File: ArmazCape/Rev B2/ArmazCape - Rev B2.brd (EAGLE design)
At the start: 85 x 70.5 mm, 167 parts, among them J2 85505-5113, Q1 32.768kHz, 12.5pF, Q2 ASE, Q4 IRLML6344TRPBF, Q5 IRLML6344TRPBF, U1 L7985A, U13 L7985A, U19 DS1307ZN+, U20 24AA256-I/SN, U5 CD4050BD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

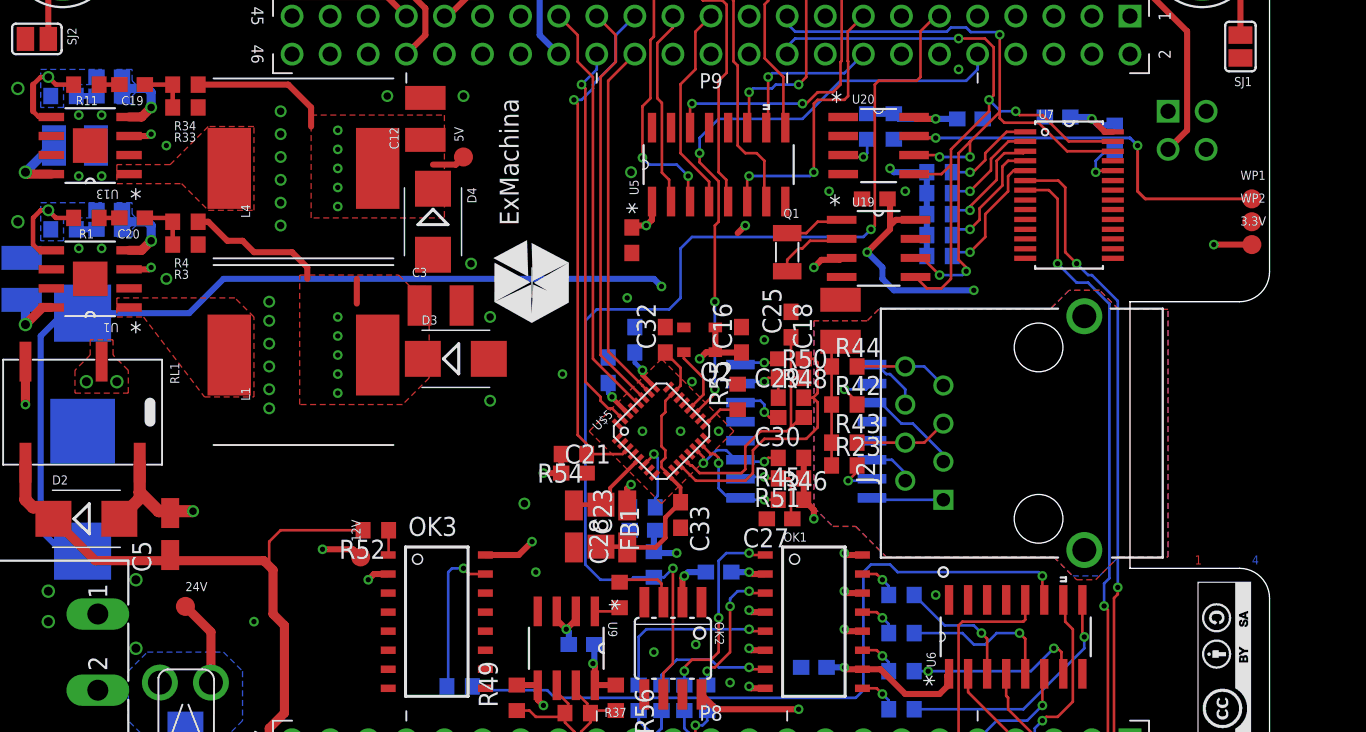
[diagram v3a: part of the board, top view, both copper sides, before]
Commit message: Updated ArmazCape - Rev B2: Silkscreen for production Fixed bad Rev number on board.
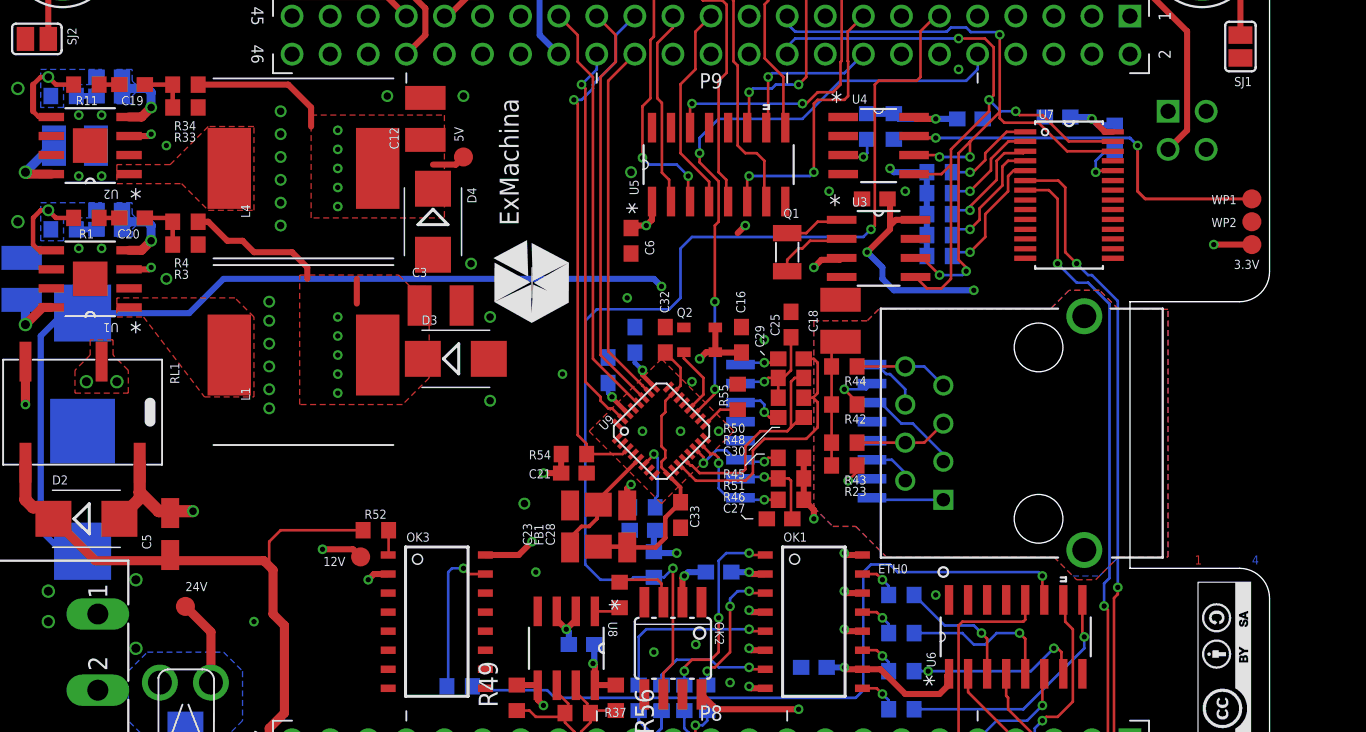
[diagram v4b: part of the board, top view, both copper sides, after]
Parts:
- removed U$5: KSZ8851SNLI, Micrel_By_element14_Batch_1:QFN50P500X500X85-32L
- added U8: SN65HVD08D, ti:SOIC127P600X175-8N
- U9: value SN65HVD08D -> KSZ8851SNLI; device ti:SOIC127P600X175-8N -> Micrel_By_element14_Batch_1:QFN50P500X500X85-32L
- moved U$3 228.5 mm to (-83.3, -55.6)
- moved U9 15.8 mm to (44.5, 34.3), turned to 45 degrees
- moved C23 0.25 mm to (38.4, 27.9), turned to 90 degrees
- moved FB1 0.18 mm to (40.2, 27.9)
- moved C6 0.07 mm to (42.4, 47.0)
- renumbered J2 to ETH0, U$4 to M1, U13 to U2, U19 to U3, U20 to U4
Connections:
- net +3V3: now also U9.25, U9.30; no longer U$5.25, U$5.30
- net +5V/1: now also U8.8; no longer U9.8
- net DMX0-A: now also U8.6; no longer U9.6
- net DMX0-B: now also U8.7; no longer U9.7
- net GND: now also U9.13, U9.18, U9.22, U9.24, U9.29, U9.4, U9.8; no longer U$5.13, U$5.18, U$5.22, U$5.24, U$5.29, U$5.4, U$5.8
- net GND1: now also U8.2, U8.3, U8.5; no longer U9.2, U9.3, U9.5
- net KSZ_X1: now also U9.20; no longer U$5.20
- net N$2000: now also U9.11; no longer U$5.11
- net N$27: now also U8.1; no longer U9.1
- net N$300: now also U9.12; no longer U$5.12
- net N$38: now also U9.17; no longer U$5.17
- net N$4200: now also U9.14; no longer U$5.14
- net N$4400: now also U9.15; no longer U$5.15
- net N$52: now also U9.6; no longer U$5.6
- net SPI1_CS0: now also U9.26; no longer U$5.26
- net SPI1_INT: now also U9.3; no longer U$5.3
- net SPI1_MISO: now also U9.27; no longer U$5.27
- net SPI1_MOSI: now also U9.31; no longer U$5.31
- net SPI1_SCLK: now also U9.28; no longer U$5.28
- net SYS_RESET: now also U9.19; no longer U$5.19
- net VDD18CORE: now also U9.5; no longer U$5.5
- net VDD18PLL: now also U9.23, U9.9; no longer U$5.23, U$5.9
- net VDD_A3.3: now also U9.16; no longer U$5.16
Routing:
- net VDD18CORE: track 5.88 -> 8.06 mm
- removed copper zone on layer 15, net GND
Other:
- board text added: "ArmazCape Rev B2"
- board text removed: "ArmazCape Rev B1"

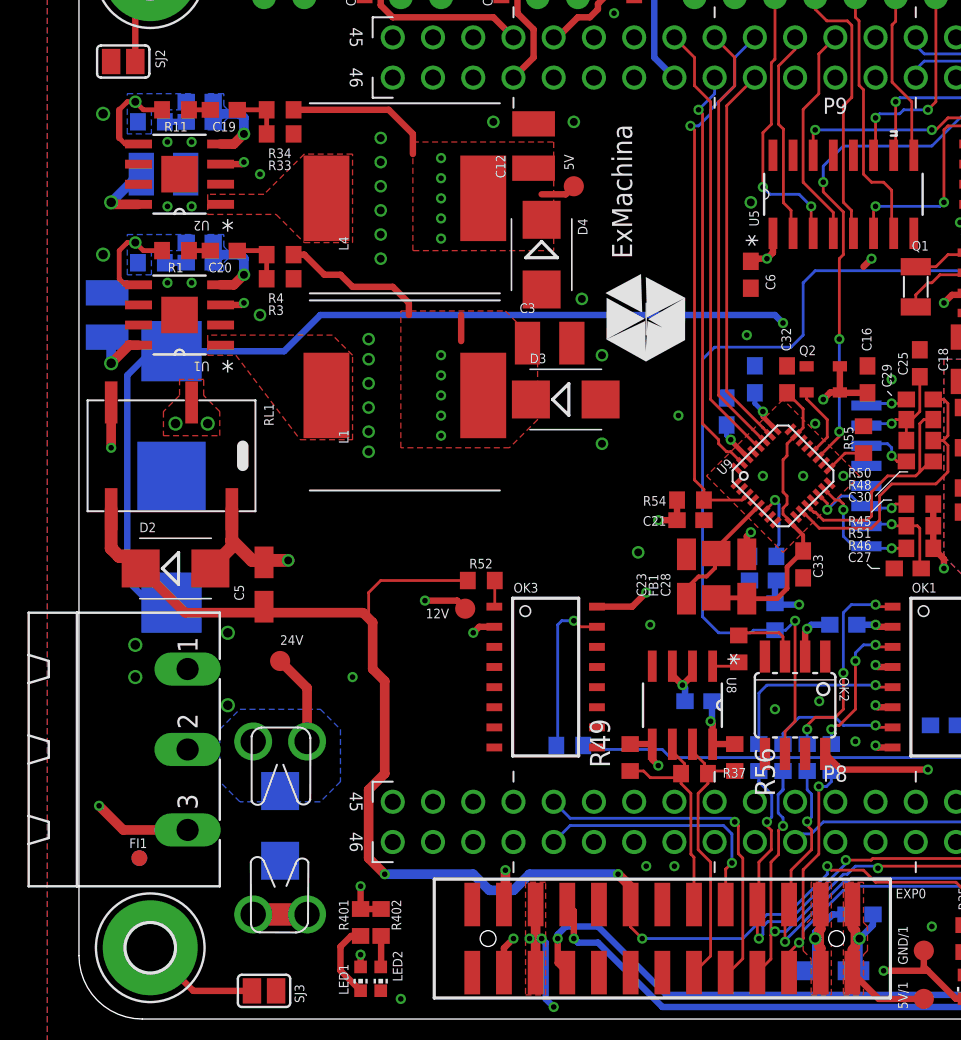
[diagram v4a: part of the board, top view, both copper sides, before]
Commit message: Fixed OAR in DRC (EuroCircuits)
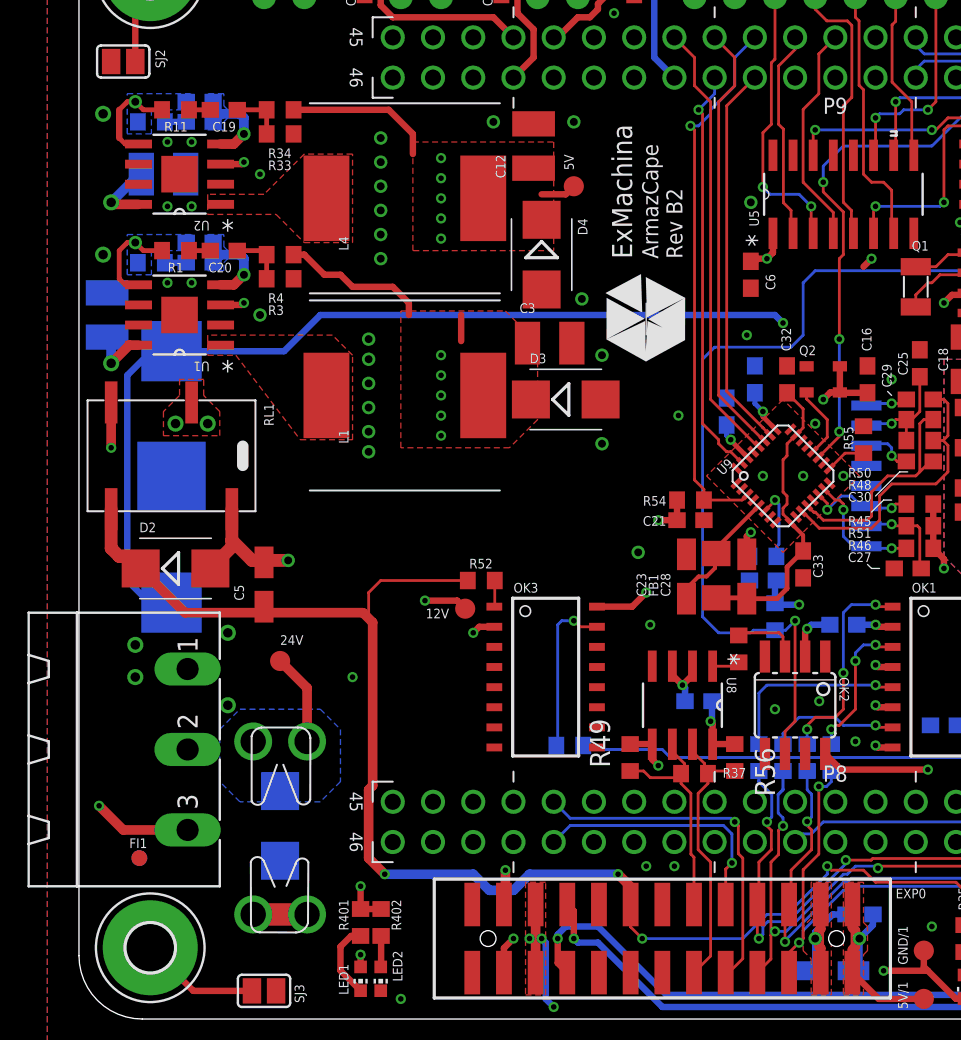
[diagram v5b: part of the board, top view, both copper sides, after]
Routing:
- net DV0: track 92.6 -> 92.0 mm
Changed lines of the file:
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@@
 <layer number="49" name="Reference" color="7" fill="1" visible="no" active="yes"/>
 <layer number="50" name="dxf" color="7" fill="1" visible="no" active="no"/>
-<layer number="51" name="tDocu" color="7" fill="1" visible="yes" active="yes"/>
+<layer number="51" name="tDocu" color="7" fill="1" visible="no" active="yes"/>
 <layer number="52" name="bDocu" color="7" fill="1" visible="no" active="yes"/>
 <layer number="53" name="tGND_GNDA" color="7" fill="1" visible="no" active="no"/>
@@
 Creatives Commons
 CC BY-SA</text>
-<text x="35.56" y="48.006" size="1.016" layer="51" font="vector" ratio="10" rot="R90" align="top-left">ArmazCape
+<text x="35.56" y="48.006" size="1.016" layer="21" font="vector" ratio="10" rot="R90" align="top-left">ArmazCape
 Rev B2</text>
 <text x="0" y="-1.27" size="1.9304" layer="51" font="vector" ratio="10" align="top-left">Top side</text>
@@
 <param name="rvPadInner" value="0.25"/>
 <param name="rvPadBottom" value="0.25"/>
-<param name="rvViaOuter" value="0.25"/>
-<param name="rvViaInner" value="0.25"/>
+<param name="rvViaOuter" value="0.35"/>
+<param name="rvViaInner" value="0.35"/>
 <param name="rvMicroViaOuter" value="0"/>
 <param name="rvMicroViaInner" value="0"/>
@@
 <param name="checkFont" value="1"/>
 <param name="checkRestrict" value="1"/>
-<param name="useDiameter" value="13"/>
+<param name="useDiameter" value="31"/>
 <param name="maxErrors" value="50"/>
 </designrules>
@@
 <wire x1="19.304" y1="9.144" x2="18.288" y2="10.16" width="0.6096" layer="1"/>
 <wire x1="18.288" y1="10.16" x2="18.288" y2="14.478" width="0.6096" layer="1"/>
-<wire x1="18.288" y1="14.478" x2="19.304" y2="15.494" width="0.6096" layer="1"/>
-<wire x1="19.304" y1="15.494" x2="19.304" y2="21.336" width="0.6096" layer="1"/>
-<wire x1="19.304" y1="21.336" x2="18.542" y2="22.098" width="0.6096" layer="1"/>
-<wire x1="18.542" y1="22.098" x2="18.542" y2="25.042" width="0.6096" layer="1"/>
+<wire x1="18.288" y1="14.478" x2="18.542" y2="14.732" width="0.6096" layer="1"/>
+<wire x1="18.542" y1="14.732" x2="18.542" y2="25.042" width="0.6096" layer="1"/>
 <wire x1="18.542" y1="25.042" x2="17.93" y2="25.654" width="0.6096" layer="1"/>
 <via x="19.304" y="9.144" extent="1-16" drill="0.35"/>

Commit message: Added GERBER files for ArmazCape Rev B3
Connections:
- net N$4: now also M1.8; no longer M1.6
- net N$4200: now also M1.1; no longer M1.3
- net N$4400: now also M1.3; no longer M1.1
- net N$51: now also M1.6; no longer M1.8
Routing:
- net N$4400: track 7.94 -> 12.7 mm
- net N$4200: track 7.01 -> 11.5 mm
- net N$51: track 2.68 -> 5.17 mm
- net N$4: track 3.33 -> 5.57 mm
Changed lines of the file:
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@@
 <setting verticaltext="up"/>
 </settings>
-<grid distance="10" unitdist="mil" unit="mil" style="lines" multiple="5" display="yes" altdistance="1" altunitdist="mil" altunit="mil"/>
+<grid distance="50" unitdist="mil" unit="mil" style="dots" multiple="2" display="yes" altdistance="25" altunitdist="mil" altunit="mil"/>
 <layers>
-<layer number="1" name="Top" color="43" fill="1" visible="yes" active="yes"/>
-<layer number="2" name="Route2" color="32" fill="1" visible="no" active="yes"/>
+<layer number="1" name="Top" color="16" fill="1" visible="yes" active="yes"/>
+<layer number="2" name="Route2" color="17" fill="1" visible="no" active="yes"/>
 <layer number="3" name="Route3" color="4" fill="3" visible="no" active="no"/>
 <layer number="14" name="Route14" color="1" fill="6" visible="no" active="no"/>
-<layer number="15" name="Route15" color="38" fill="1" visible="no" active="yes"/>
-<layer number="16" name="Bottom" color="17" fill="1" visible="no" active="yes"/>
-<layer number="17" name="Pads" color="2" fill="1" visible="yes" active="yes"/>
-<layer number="18" name="Vias" color="2" fill="1" visible="yes" active="yes"/>
+<layer number="15" name="Route15" color="19" fill="1" visible="no" active="yes"/>
+<layer number="16" name="Bottom" color="21" fill="1" visible="yes" active="yes"/>
+<layer number="17" name="Pads" color="18" fill="1" visible="yes" active="yes"/>
+<layer number="18" name="Vias" color="38" fill="1" visible="yes" active="yes"/>
 <layer number="19" name="Unrouted" color="6" fill="1" visible="yes" active="yes"/>
-<layer number="20" name="Dimension" color="26" fill="1" visible="yes" active="yes"/>
-<layer number="21" name="tPlace" color="7" fill="1" visible="yes" active="yes"/>
-<layer number="22" name="bPlace" color="7" fill="1" visible="no" active="yes"/>
-<layer number="23" name="tOrigins" color="15" fill="1" visible="yes" active="yes"/>
-<layer number="24" name="bOrigins" color="15" fill="1" visible="no" active="yes"/>
-<layer number="25" name="tNames" color="7" fill="1" visible="yes" active="yes"/>
-<layer number="26" name="bNames" color="7" fill="1" visible="no" active="yes"/>
-<layer number="27" name="tValues" color="7" fill="1" visible="yes" active="yes"/>
-<layer number="28" name="bValues" color="7" fill="1" visible="no" active="yes"/>
+<layer number="20" name="Dimension" color="7" fill="1" visible="yes" active="yes"/>
+<layer number="21" name="tPlace" color="55" fill="1" visible="no" active="yes"/>
+<layer number="22" name="bPlace" color="54" fill="1" visible="yes" active="yes"/>
+<layer number="23" name="tOrigins" color="15" fill="1" visible="no" active="yes"/>
+<layer number="24" name="bOrigins" color="15" fill="1" visible="yes" active="yes"/>
+<layer number="25" name="tNames" color="55" fill="1" visible="no" active="yes"/>
+<layer number="26" name="bNames" color="54" fill="1" visible="yes" active="yes"/>
+<layer number="27" name="tValues" color="53" fill="1" visible="no" active="yes"/>
+<layer number="28" name="bValues" color="52" fill="1" visible="yes" active="yes"/>
 <layer number="29" name="tStop" color="7" fill="3" visible="no" active="yes"/>
 <layer number="30" name="bStop" color="7" fill="6" visible="no" active="yes"/>
@@
 <layer number="38" name="bTest" color="7" fill="1" visible="no" active="yes"/>
 <layer number="39" name="tKeepout" color="4" fill="11" visible="no" active="yes"/>
-<layer number="40" name="bKeepout" color="1" fill="11" visible="no" active="yes"/>
+<layer number="40" name="bKeepout" color="3" fill="11" visible="no" active="yes"/>
 <layer number="41" name="tRestrict" color="4" fill="10" visible="no" active="yes"/>
-<layer number="42" name="bRestrict" color="1" fill="10" visible="no" active="yes"/>
+<layer number="42" name="bRestrict" color="3" fill="10" visible="no" active="yes"/>
 <layer number="43" name="vRestrict" color="2" fill="10" visible="no" active="yes"/>
-<layer number="44" name="Drills" color="7" fill="1" visible="no" active="yes"/>
-<layer number="45" name="Holes" color="7" fill="1" visible="no" active="yes"/>
-<layer number="46" name="Milling" color="3" fill="1" visible="no" active="yes"/>
-<layer number="47" name="Measures" color="7" fill="1" visible="yes" active="yes"/>
-<layer number="48" name="Document" color="7" fill="1" visible="no" active="yes"/>
-<layer number="49" name="Reference" color="7" fill="1" visible="no" active="yes"/>
+<layer number="44" name="Drills" color="16" fill="1" visible="no" active="yes"/>
+<layer number="45" name="Holes" color="35" fill="1" visible="no" active="yes"/>
+<layer number="46" name="Milling" color="35" fill="1" visible="no" active="yes"/>
+<layer number="47" name="Measures" color="21" fill="1" visible="yes" active="yes"/>
+<layer number="48" name="Document" color="24" fill="1" visible="no" active="yes"/>
+<layer number="49" name="Reference" color="48" fill="1" visible="no" active="yes"/>
 <layer number="50" name="dxf" color="7" fill="1" visible="no" active="no"/>
-<layer number="51" name="tDocu" color="7" fill="1" visible="no" active="yes"/>
-<layer number="52" name="bDocu" color="7" fill="1" visible="no" active="yes"/>
+<layer number="51" name="tDocu" color="55" fill="1" visible="no" active="yes"/>
+<layer number="52" name="bDocu" color="54" fill="1" visible="yes" active="yes"/>
 <layer number="53" name="tGND_GNDA" color="7" fill="1" visible="no" active="no"/>
 <layer number="54" name="bGND_GNDA" color="7" fill="1" visible="no" active="no"/>
@@
 <layer number="100" name="Mechanical" color="7" fill="1" visible="yes" active="yes"/>
 <layer number="101" name="Patch_Top" color="7" fill="1" visible="no" active="yes"/>
-<layer number="102" name="Vscore" color="7" fill="1" visible="no" active="yes"/>
+<layer number="102" name="Vscore" color="13" fill="1" visible="no" active="yes"/>
 <layer number="103" name="Top_middle" color="7" fill="1" visible="no" active="yes"/>
 <layer number="104" name="Name" color="7" fill="1" visible="no" active="yes"/>
@@
 <wire x1="47.244" y1="32.1564" x2="47.244" y2="32.55665625" width="0.1778" layer="1"/>
 <wire x1="47.244" y1="32.55665625" x2="46.68445625" y2="33.1162" width="0.1778" layer="1"/>
-<contactref element="M1" pad="3"/>
+<contactref element="M1" pad="1"/>
 <wire x1="52.236" y1="32.512" x2="51.562" y2="32.512" width="0.1778" layer="1"/>
 <wire x1="51.562" y1="32.512" x2="51.308" y2="32.258" width="0.1778" layer="1"/>
 <via x="51.308" y="32.258" extent="1-16" drill="0.35"/>
 <wire x1="51.308" y1="32.258" x2="49.844" y2="32.258" width="0.1778" layer="16"/>
-<wire x1="49.844" y1="32.258" x2="49.717" y2="32.385" width="0.1778" layer="16"/>
-<wire x1="49.717" y1="32.385" x2="49.403" y2="32.385" width="0.1778" layer="16"/>
+<wire x1="49.844" y1="32.258" x2="49.717" y2="29.845" width="0.1778" layer="16"/>
+<wire x1="49.717" y1="29.845" x2="49.403" y2="32.385" width="0.1778" layer="16"/>
 <wire x1="49.403" y1="32.385" x2="48.768" y2="33.02" width="0.1778" layer="16"/>
 <wire x1="48.768" y1="33.02" x2="48.1076" y2="33.02" width="0.1778" layer="16"/>
@@
 <signal name="N$51">
 <contactref element="C29" pad="2"/>
-<contactref element="M1" pad="8"/>
+<contactref element="M1" pad="6"/>
 <via x="51.308" y="38.862" extent="1-16" drill="0.35"/>
 <wire x1="51.308" y1="38.862" x2="49.844" y2="38.862" width="0.1778" layer="16"/>
-<wire x1="49.844" y1="38.862" x2="49.717" y2="38.735" width="0.1778" layer="16"/>
+<wire x1="49.844" y1="38.862" x2="49.717" y2="36.195" width="0.1778" layer="16"/>
 <wire x1="51.308" y1="38.862" x2="51.982" y2="38.862" width="0.1778" layer="1"/>
 <wire x1="51.982" y1="38.862" x2="52.236" y2="39.116" width="0.1778" layer="1"/>
@@
 <contactref element="R46" pad="1"/>
 <contactref element="U9" pad="15"/>
-<contactref element="M1" pad="1"/>
+<contactref element="M1" pad="3"/>
 <wire x1="47.038009375" y1="33.469753125" x2="47.7417625" y2="32.766" width="0.1778" layer="1"/>
 <wire x1="47.7417625" y1="32.766" x2="48.006" y2="32.766" width="0.1778" layer="1"/>
@@
 <wire x1="48.26" y1="30.48" x2="48.768" y2="29.972" width="0.1778" layer="16"/>
 <wire x1="48.768" y1="29.972" x2="49.59" y2="29.972" width="0.1778" layer="16"/>
-<wire x1="49.59" y1="29.972" x2="49.717" y2="29.845" width="0.1778" layer="16"/>
+<wire x1="49.59" y1="29.972" x2="49.717" y2="32.385" width="0.1778" layer="16"/>
 <wire x1="52.236" y1="29.718" x2="51.308" y2="29.718" width="0.1778" layer="1"/>
 <via x="51.308" y="29.718" extent="1-16" drill="0.35"/>
 <wire x1="51.308" y1="29.718" x2="49.844" y2="29.718" width="0.1778" layer="16"/>
-<wire x1="49.844" y1="29.718" x2="49.717" y2="29.845" width="0.1778" layer="16"/>
+<wire x1="49.844" y1="29.718" x2="49.717" y2="32.385" width="0.1778" layer="16"/>
 <wire x1="48.006" y1="32.766" x2="48.26" y2="32.512" width="0.1778" layer="1"/>
 <wire x1="48.26" y1="32.512" x2="48.26" y2="32.1564" width="0.1778" layer="1"/>
 </signal>
 <signal name="N$4">
-<contactref element="M1" pad="6"/>
+<contactref element="M1" pad="8"/>
 <contactref element="C30" pad="2"/>
 <wire x1="52.236" y1="35.2044" x2="51.6636" y2="35.2044" width="0.1778" layer="1"/>
@@
 <wire x1="51.308" y1="36.068" x2="51.054" y2="36.322" width="0.1778" layer="16"/>
 <wire x1="51.054" y1="36.322" x2="49.844" y2="36.322" width="0.1778" layer="16"/>
-<wire x1="49.844" y1="36.322" x2="49.717" y2="36.195" width="0.1778" layer="16"/>
+<wire x1="49.844" y1="36.322" x2="49.717" y2="38.735" width="0.1778" layer="16"/>
 </signal>
 <signal name="N$52">
